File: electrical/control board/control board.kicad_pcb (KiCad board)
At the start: 4 copper layers, 72.4 x 149.8 mm, 54 parts, among them J1 analog_extra, J10 Motor_2, J11 Motor_3, J12 Motor_4, J13 Motor_5, J14 Motor_6, J15 Motor_7, J16 Motor_8, J2 Programming_Header, J3 Conn_01x08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

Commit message: stuff
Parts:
- removed C1: 0.1uF, Capacitor_SMD:C_0603_1608Metric_Pad1.05x0.95mm_HandSolder
- removed C15, C17, C18: .1uF, Capacitor_SMD:C_0603_1608Metric_Pad1.05x0.95mm_HandSolder
- removed C2, C3: 30pF, Capacitor_SMD:C_0603_1608Metric_Pad1.05x0.95mm_HandSolder
- removed C4: 1uF, Capacitor_SMD:C_0603_1608Metric_Pad1.05x0.95mm_HandSolder
- removed R1, R2: 4.7k, Resistor_SMD:R_0603_1608Metric_Pad1.05x0.95mm_HandSolder
- removed R10, R11, R17, R18, R19, R9: R_Small, Resistor_SMD:R_0603_1608Metric_Pad1.05x0.95mm_HandSolder
- removed R12, R13, R3, R4, R5, R7: 10k, Resistor_SMD:R_0603_1608Metric_Pad1.05x0.95mm_HandSolder
- removed R14: 12k, Resistor_SMD:R_0603_1608Metric_Pad1.05x0.95mm_HandSolder
- removed R15: 100k, Resistor_SMD:R_0603_1608Metric_Pad1.05x0.95mm_HandSolder
- removed R16: 3.6k, Resistor_SMD:R_0603_1608Metric_Pad1.05x0.95mm_HandSolder
- removed R8: 56k, Resistor_SMD:R_0603_1608Metric_Pad1.05x0.95mm_HandSolder
- C14, J2, Q2, U2, U7: moved to B.Cu
- moved U7 85.8 mm to (64.1, 69.2), turned to 90 degrees
- moved Q2 68.9 mm to (58.4, 70.5)
- moved C14 66.9 mm to (92.1, 88.9), turned to 270 degrees
- moved J2 29.5 mm to (86.4, 78.7)
- moved J1 24.8 mm to (90.2, 118.1)
- moved J5 8.61 mm to (92.1, 148.2)
- moved J10 8.39 mm to (87.8, 148.2)
- moved U2 8.26 mm to (75.6, 59.7)
- moved J11 8.17 mm to (83.5, 148.2)
- moved J12 7.95 mm to (79.2, 148.2)
- moved J13 7.74 mm to (74.9, 148.2)
- moved J14 7.07 mm to (70.6, 148.2)
- moved J15 6.07 mm to (66.3, 148.2)
- moved J16 5.99 mm to (62.0, 148.2)
- moved C9 1.42 mm to (74.3, 87.6), turned to 180 degrees
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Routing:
- net Net-(J5-Pad3): track 0.00 -> 80.9 mm, vias 0 -> 2
- net Net-(J10-Pad3): track 0.00 -> 75.3 mm, vias 0 -> 2
- net Net-(J12-Pad3): track 0.00 -> 75.2 mm
- net Net-(J15-Pad3): track 0.00 -> 74.7 mm, vias 0 -> 2
- net Net-(J13-Pad3): track 0.00 -> 73.9 mm, vias 0 -> 2
- net Net-(J11-Pad3): track 0.00 -> 72.8 mm, vias 0 -> 2
- net Net-(J16-Pad3): track 0.00 -> 71.9 mm, vias 0 -> 2
- net Net-(J14-Pad3): track 0.00 -> 71.4 mm, vias 0 -> 2
- net /NRST: track 0.00 -> 47.7 mm, vias 0 -> 1
- net /SENSOR_RX: track 0.00 -> 35.5 mm, vias 0 -> 2
- net GND: track 0.00 -> 35.3 mm, vias 7 -> 13
- net /SENSOR_RE: track 0.00 -> 34.1 mm, vias 0 -> 2
- net +3V3: track 56.3 -> 23.0 mm, vias 0 -> 9
- net /SENSOR_TX: track 0.00 -> 32.9 mm, vias 0 -> 2
- net /SENSOR_DE: track 0.00 -> 32.3 mm, vias 0 -> 2
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- added copper zone on In1.Cu, net +3V3
- added copper zone on In2.Cu, net GND
- removed copper zone on In2.Cu, net +3V3
- removed copper zone on In1.Cu, net GND

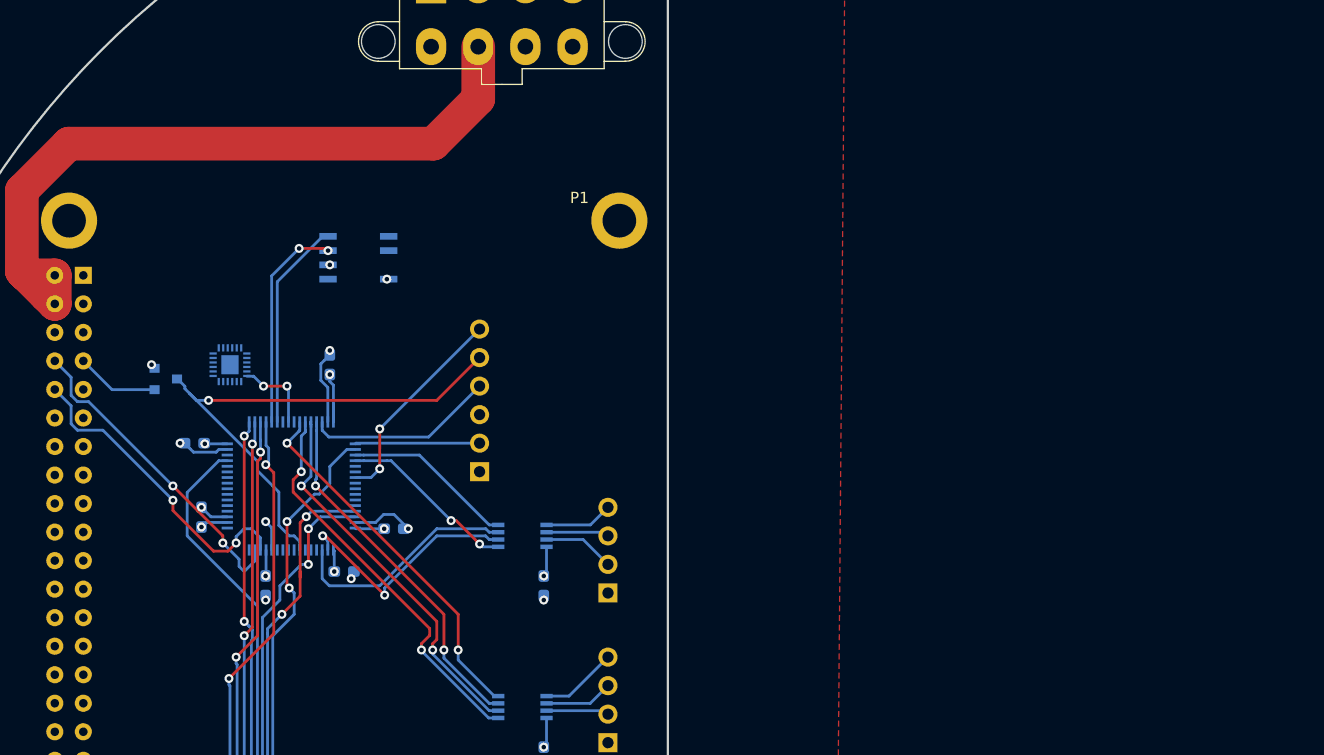
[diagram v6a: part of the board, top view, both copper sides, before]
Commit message: routed voltage measurement
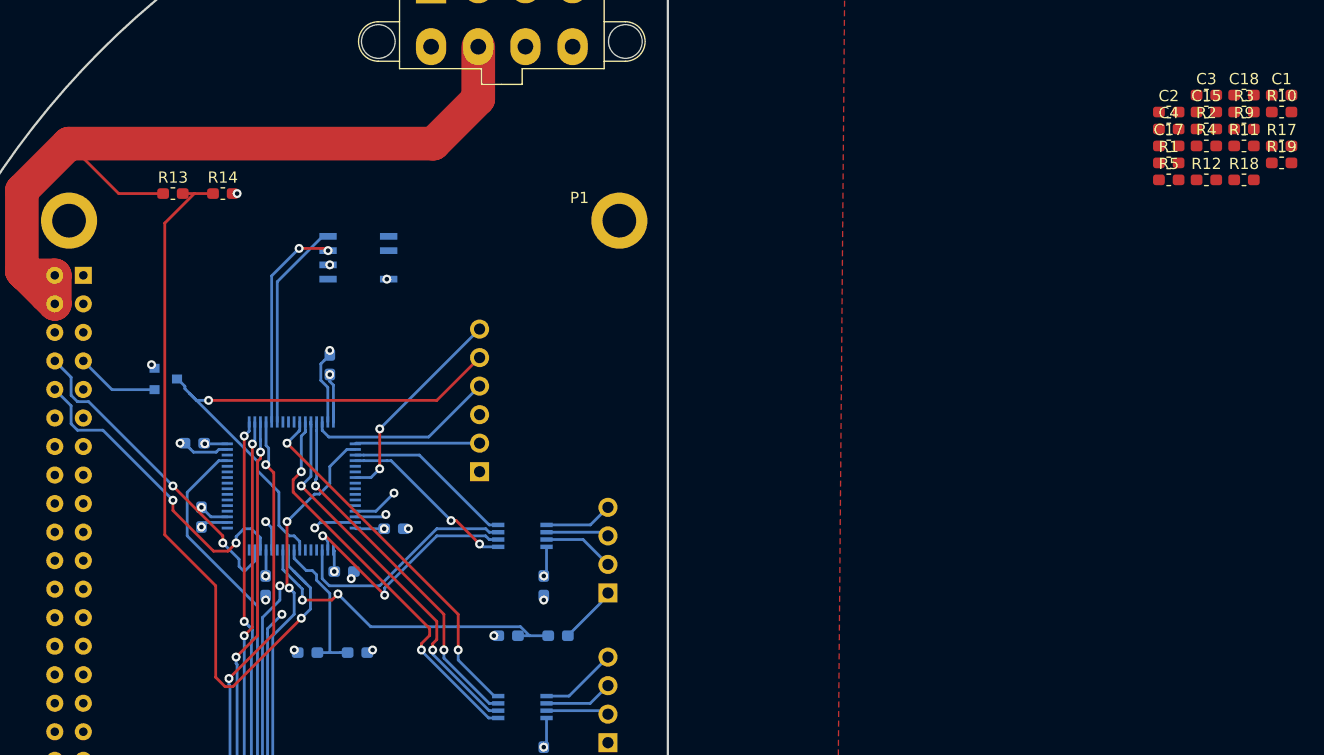
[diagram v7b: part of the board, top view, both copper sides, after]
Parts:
- removed U7: ICM20648, footprints:ICM-20648
- added C1: 0.1uF, Capacitor_SMD:C_0603_1608Metric_Pad1.05x0.95mm_HandSolder, F.Cu at (157.8, 45.2)
- added C15: .1uF, Capacitor_SMD:C_0603_1608Metric_Pad1.05x0.95mm_HandSolder, F.Cu at (151.1, 46.7)
- added C17: .1uF, Capacitor_SMD:C_0603_1608Metric_Pad1.05x0.95mm_HandSolder, F.Cu at (147.7, 49.7)
- added C18: .1uF, Capacitor_SMD:C_0603_1608Metric_Pad1.05x0.95mm_HandSolder, F.Cu at (154.4, 45.2)
- added C2: 30pF, Capacitor_SMD:C_0603_1608Metric_Pad1.05x0.95mm_HandSolder, F.Cu at (147.7, 46.7)
- added C3: 30pF, Capacitor_SMD:C_0603_1608Metric_Pad1.05x0.95mm_HandSolder, F.Cu at (151.1, 45.2)
- added C4: 1uF, Capacitor_SMD:C_0603_1608Metric_Pad1.05x0.95mm_HandSolder, F.Cu at (147.7, 48.2)
- added R1: 4.7k, Resistor_SMD:R_0603_1608Metric_Pad1.05x0.95mm_HandSolder, F.Cu at (147.7, 51.2)
- added R10: R_Small, Resistor_SMD:R_0603_1608Metric_Pad1.05x0.95mm_HandSolder, F.Cu at (157.8, 46.7)
- added R11: R_Small, Resistor_SMD:R_0603_1608Metric_Pad1.05x0.95mm_HandSolder, F.Cu at (154.4, 49.7)
- added R12: 10k, Resistor_SMD:R_0603_1608Metric_Pad1.05x0.95mm_HandSolder, F.Cu at (151.1, 52.8)
- added R13: 10k, Resistor_SMD:R_0603_1608Metric_Pad1.05x0.95mm_HandSolder, F.Cu at (59.1, 54.0)
- added R14: 12k, Resistor_SMD:R_0603_1608Metric_Pad1.05x0.95mm_HandSolder, F.Cu at (63.5, 54.0)
- added R15: 100k, Resistor_SMD:R_0603_1608Metric_Pad1.05x0.95mm_HandSolder, B.Cu at (93.3, 93.3)
- added R16: 3.6k, Resistor_SMD:R_0603_1608Metric_Pad1.05x0.95mm_HandSolder, B.Cu at (88.9, 93.3)
- added R17: R_Small, Resistor_SMD:R_0603_1608Metric_Pad1.05x0.95mm_HandSolder, F.Cu at (157.8, 49.7)
- added R18: R_Small, Resistor_SMD:R_0603_1608Metric_Pad1.05x0.95mm_HandSolder, F.Cu at (154.4, 52.8)
- added R19: R_Small, Resistor_SMD:R_0603_1608Metric_Pad1.05x0.95mm_HandSolder, F.Cu at (157.8, 51.2)
- added R2: 4.7k, Resistor_SMD:R_0603_1608Metric_Pad1.05x0.95mm_HandSolder, F.Cu at (151.1, 48.2)
- added R3: 10k, Resistor_SMD:R_0603_1608Metric_Pad1.05x0.95mm_HandSolder, F.Cu at (154.4, 46.7)
- added R4: 10k, Resistor_SMD:R_0603_1608Metric_Pad1.05x0.95mm_HandSolder, F.Cu at (151.1, 49.7)
- added R5: 10k, Resistor_SMD:R_0603_1608Metric_Pad1.05x0.95mm_HandSolder, F.Cu at (147.7, 52.8)
- added R7: 10k, Resistor_SMD:R_0603_1608Metric_Pad1.05x0.95mm_HandSolder, B.Cu at (71.0, 94.8)
- added R8: 56k, Resistor_SMD:R_0603_1608Metric_Pad1.05x0.95mm_HandSolder, B.Cu at (75.5, 94.8)
- added R9: R_Small, Resistor_SMD:R_0603_1608Metric_Pad1.05x0.95mm_HandSolder, F.Cu at (154.4, 48.2)
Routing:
- net /5V_MEASURE: track 0.00 -> 67.9 mm, vias 0 -> 1
- net /48V_MEASURE: track 0.00 -> 29.9 mm, vias 0 -> 2
- net /3.3V_MEASURE: track 0.00 -> 13.5 mm
- net +5V: track 65.6 -> 75.8 mm
- net /ICM_SDA: track 7.19 -> 0.00 mm, vias 2 -> 0
- net Net-(J10-Pad3): track 75.3 -> 82.4 mm
- net +48V: track 0.00 -> 5.29 mm
- net Net-(J11-Pad3): track 72.8 -> 76.6 mm
- net GND: track 35.3 -> 33.6 mm, vias 13 -> 17
- net +3V3: vias 9 -> 10

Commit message: found a crystal
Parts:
- removed C15, C17, C18: .1uF, Capacitor_SMD:C_0603_1608Metric_Pad1.05x0.95mm_HandSolder
- C1, C4, J1, R1, R2: moved to B.Cu
- moved C1 86.4 mm to (73.7, 64.8)
- moved R2 82.8 mm to (69.8, 64.1), turned to 90 degrees
- moved R1 79.3 mm to (68.6, 56.9), turned to 270 degrees
- moved C4 70.3 mm to (79.4, 64.8)
- moved J1 45.5 mm to (55.9, 88.3), turned to 0 degrees
- moved R5 7.19 mm to (145.8, 59.7)
- moved C2 4.66 mm to (145.7, 42.5)
- moved C3 3.44 mm to (150.1, 41.9)
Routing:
- net +48V: track 5.29 -> 79.4 mm
- net Net-(J1-Pad2): track 0.00 -> 13.8 mm, vias 0 -> 2
- net /HIH_SDA: track 18.7 -> 22.5 mm
- net /HIH_SCL: track 19.1 -> 22.8 mm
- net +3V3: track 23.0 -> 26.2 mm, vias 10 -> 12
- net Net-(C1-Pad1): track 0.00 -> 3.21 mm
- net GND: vias 17 -> 19
- removed copper zone on F.Cu, net GND
